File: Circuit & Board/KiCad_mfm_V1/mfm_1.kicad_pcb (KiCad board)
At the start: 2 copper layers, 59.7 x 64.5 mm, 24 parts, among them J1 Conn_01x02_Female, J2 Conn_02x03_Odd_Even, J3 Raspberry_Pi_2_3, J4 Conn_01x04_Female, J5 Conn_02x03_Odd_Even, J6 Conn_02x05_Odd_Even, Q1 10MHz, U1 PC827, U2 ATmega328-PU, U3 4093

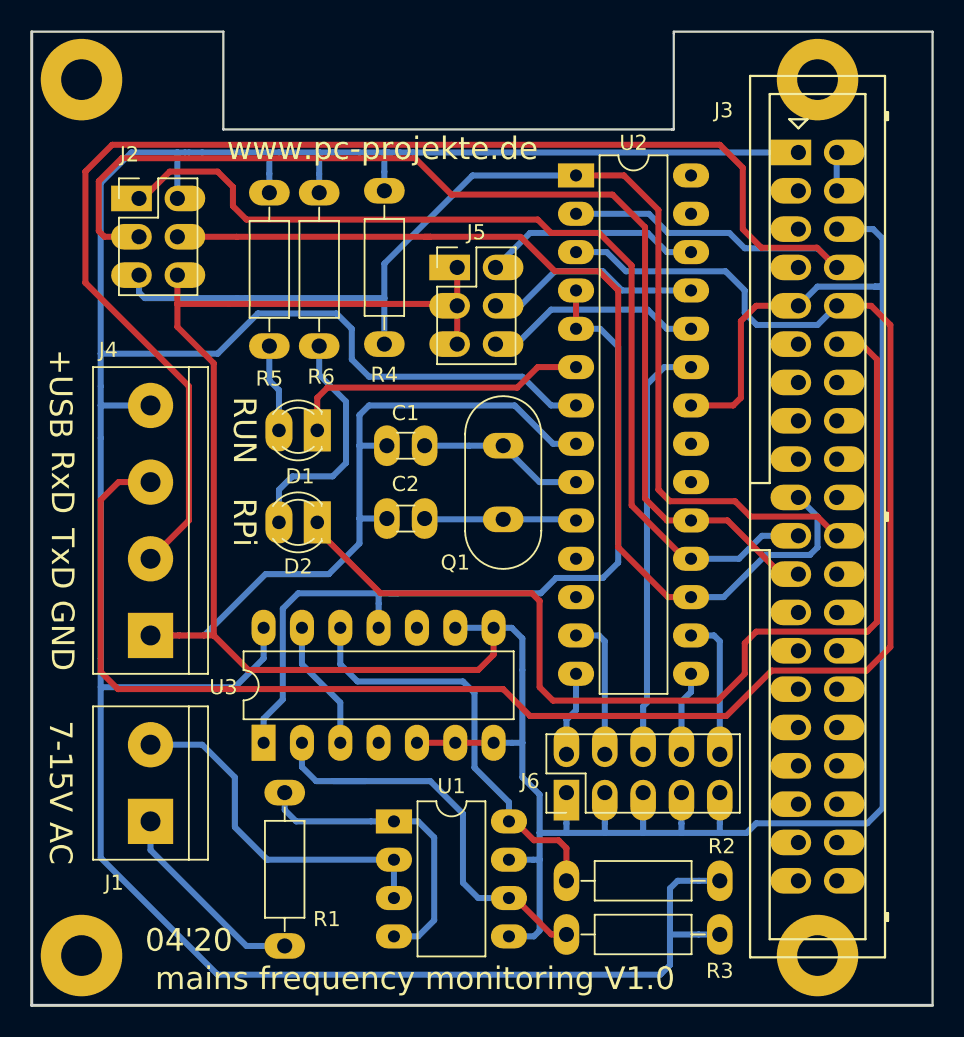
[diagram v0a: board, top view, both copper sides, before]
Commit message: Migrated to KiCAD v6 and updated footprints
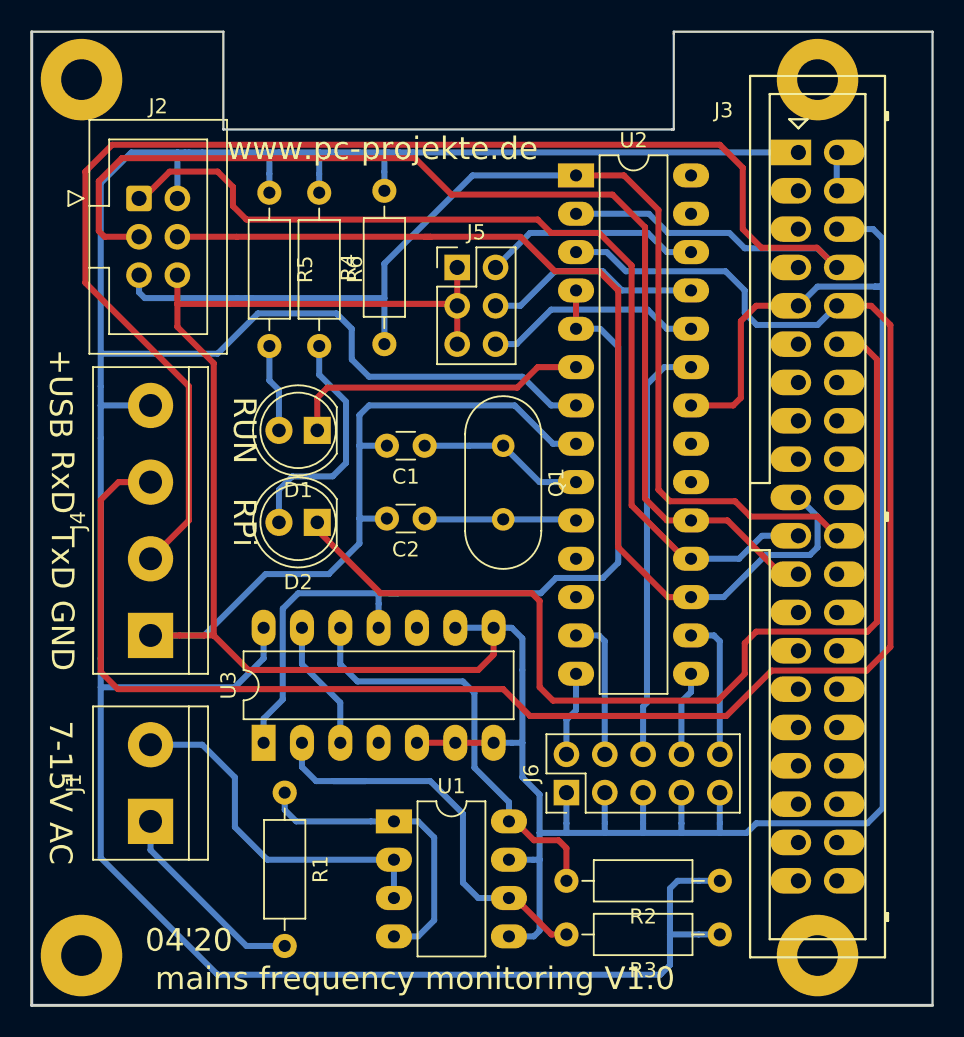
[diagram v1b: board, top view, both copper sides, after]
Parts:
- C1, C2: footprint Capacitors_THT:C_Disc_D3.0mm_W1.6mm_P2.50mm -> Capacitor_THT:C_Disc_D3.0mm_W1.6mm_P2.50mm
- D1, D2: footprint LEDs:LED_D3.0mm -> LED_THT:LED_D5.0mm_Clear
- J1: footprint Connectors_Terminal_Blocks:TerminalBlock_bornier-2_P5.08mm -> TerminalBlock:TerminalBlock_bornier-2_P5.08mm
- J2: footprint Pin_Headers:Pin_Header_Straight_2x03_Pitch2.54mm -> Connector_IDC:IDC-Header_2x03_P2.54mm_Vertical
- J4: footprint Connectors_Terminal_Blocks:TerminalBlock_bornier-4_P5.08mm -> TerminalBlock:TerminalBlock_bornier-4_P5.08mm
- J5: footprint Pin_Headers:Pin_Header_Straight_2x03_Pitch2.54mm -> Connector_PinHeader_2.54mm:PinHeader_2x03_P2.54mm_Vertical
- J6: footprint Pin_Headers:Pin_Header_Straight_2x05_Pitch2.54mm -> Connector_PinHeader_2.54mm:PinHeader_2x05_P2.54mm_Vertical
- Q1: footprint Crystals:Crystal_HC49-4H_Vertical -> Crystal:Crystal_HC49-4H_Vertical
- R1, R2, R3, R4, R5, R6: footprint Resistors_THT:R_Axial_DIN0207_L6.3mm_D2.5mm_P10.16mm_Horizontal -> Resistor_THT:R_Axial_DIN0207_L6.3mm_D2.5mm_P10.16mm_Horizontal
- U1: footprint Housings_DIP:DIP-8_W7.62mm_LongPads -> Package_DIP:DIP-8_W7.62mm_LongPads
- U2: footprint Housings_DIP:DIP-28_W7.62mm_LongPads -> Package_DIP:DIP-28_W7.62mm_LongPads
- U3: footprint Housings_DIP:DIP-14_W7.62mm_LongPads -> Package_DIP:DIP-14_W7.62mm_LongPads
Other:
- net class Default removed
